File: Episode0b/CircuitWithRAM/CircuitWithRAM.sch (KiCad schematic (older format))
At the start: 0 parts

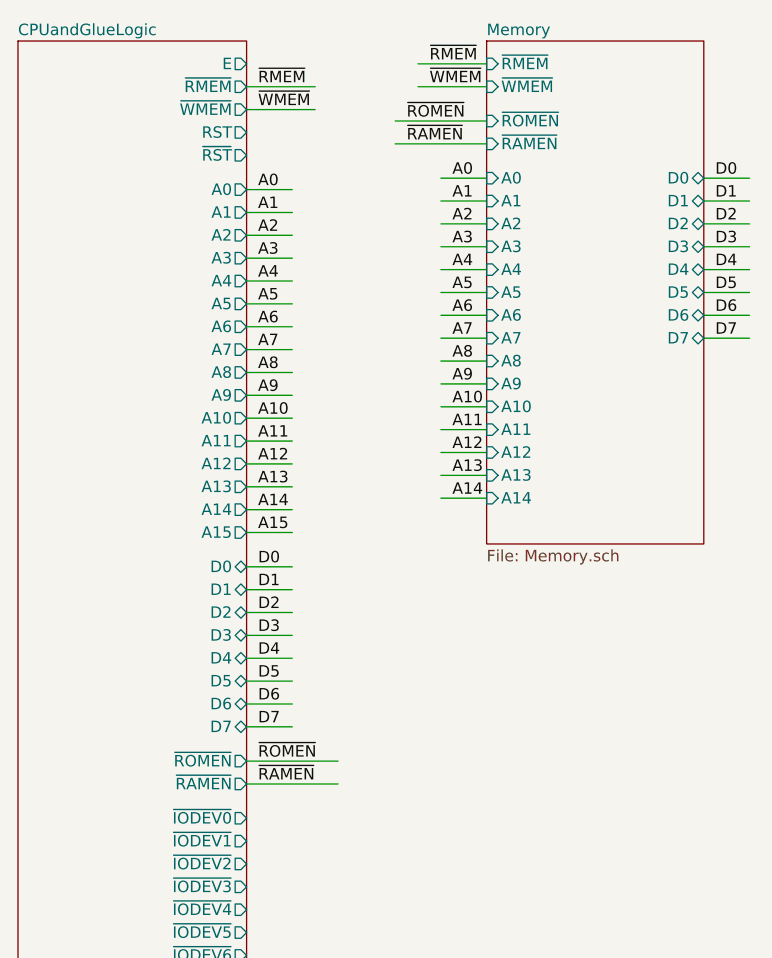
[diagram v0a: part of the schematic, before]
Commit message: just use (buffered) A15 as RAM enable
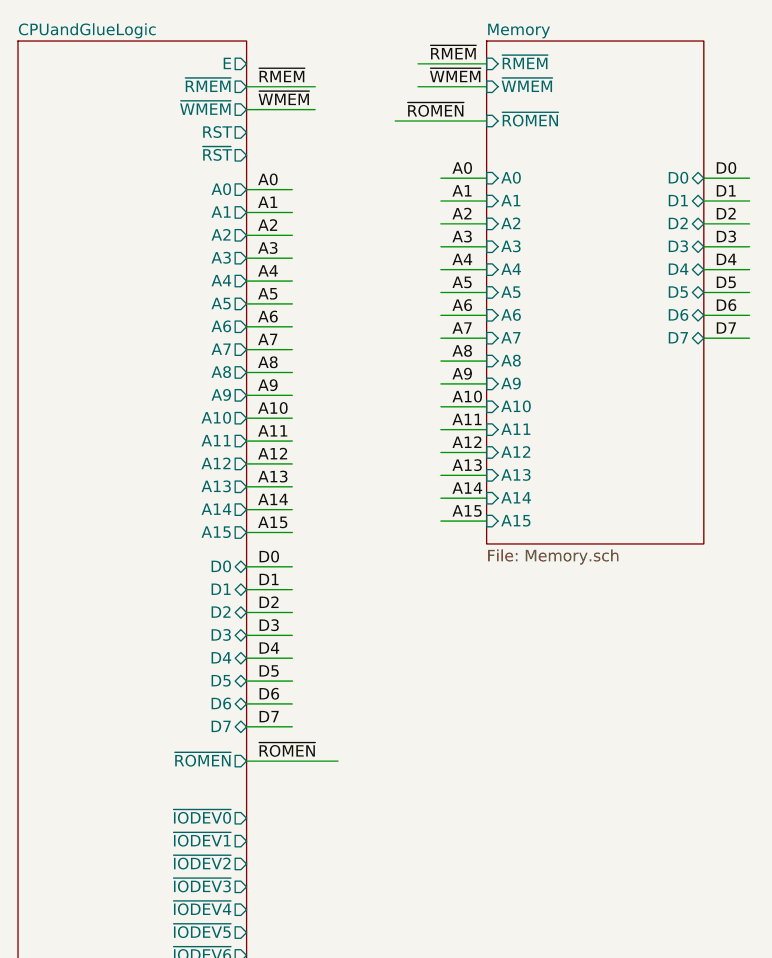
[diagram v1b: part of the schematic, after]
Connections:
- net labels removed: ~RAMEN~
- wire segments 55 -> 54
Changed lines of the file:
@@
 F46 "~IODEV15~" O R 3200 6600 50
 F47 "~ROMEN~" O R 3200 4850 50
-F48 "~RAMEN~" O R 3200 4950 50
 $EndSheet
 $Sheet
@@
 F18 "~WMEM~" I L 4250 1900 50
 F19 "~ROMEN~" I L 4250 2050 50
-F20 "~RAMEN~" I L 4250 2150 50
-F21 "D0" B R 5200 2300 50
-F22 "D1" B R 5200 2400 50
-F23 "D2" B R 5200 2500 50
-F24 "D3" B R 5200 2600 50
-F25 "D4" B R 5200 2700 50
-F26 "D5" B R 5200 2800 50
-F27 "D6" B R 5200 2900 50
-F28 "D7" B R 5200 3000 50
+F20 "D0" B R 5200 2300 50
+F21 "D1" B R 5200 2400 50
+F22 "D2" B R 5200 2500 50
+F23 "D3" B R 5200 2600 50
+F24 "D4" B R 5200 2700 50
+F25 "D5" B R 5200 2800 50
+F26 "D6" B R 5200 2900 50
+F27 "D7" B R 5200 3000 50
+F28 "A15" I L 4250 3800 50
 $EndSheet
 Wire Wire Line
@@
 Wire Wire Line
 	3200 4850 3600 4850
-Wire Wire Line
-	3200 4950 3600 4950
 Text Label 3250 4850 0    50   ~ 0
 ~ROMEN~
-Text Label 3250 4950 0    50   ~ 0
-~RAMEN~
 Wire Wire Line
 	3850 2050 4250 2050
-Wire Wire Line
-	3850 2150 4250 2150
 Text Label 3900 2050 0    50   ~ 0
 ~ROMEN~
-Text Label 3900 2150 0    50   ~ 0
-~RAMEN~
+Wire Wire Line
+	4050 3800 4250 3800
+Text Label 4100 3800 0    50   ~ 0
+A15
 $EndSCHEMATC
